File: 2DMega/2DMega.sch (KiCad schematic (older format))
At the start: 40 parts, among them J1 Conn_01x04_Male, J2 Conn_01x04_Female, J3 Conn_01x04_Male, J4 Conn_01x04_Female, P1 Power, P10 CONN_01X01, P11 CONN_01X01, P12 CONN_01X01, P13 CONN_01X01, P2 Analog, P3 Analog, P4 Digital, P5 PWM, P6 PWM, P7 Communication, P8 CONN_01X01, P9 CONN_01X01, U1 HDSP-A153

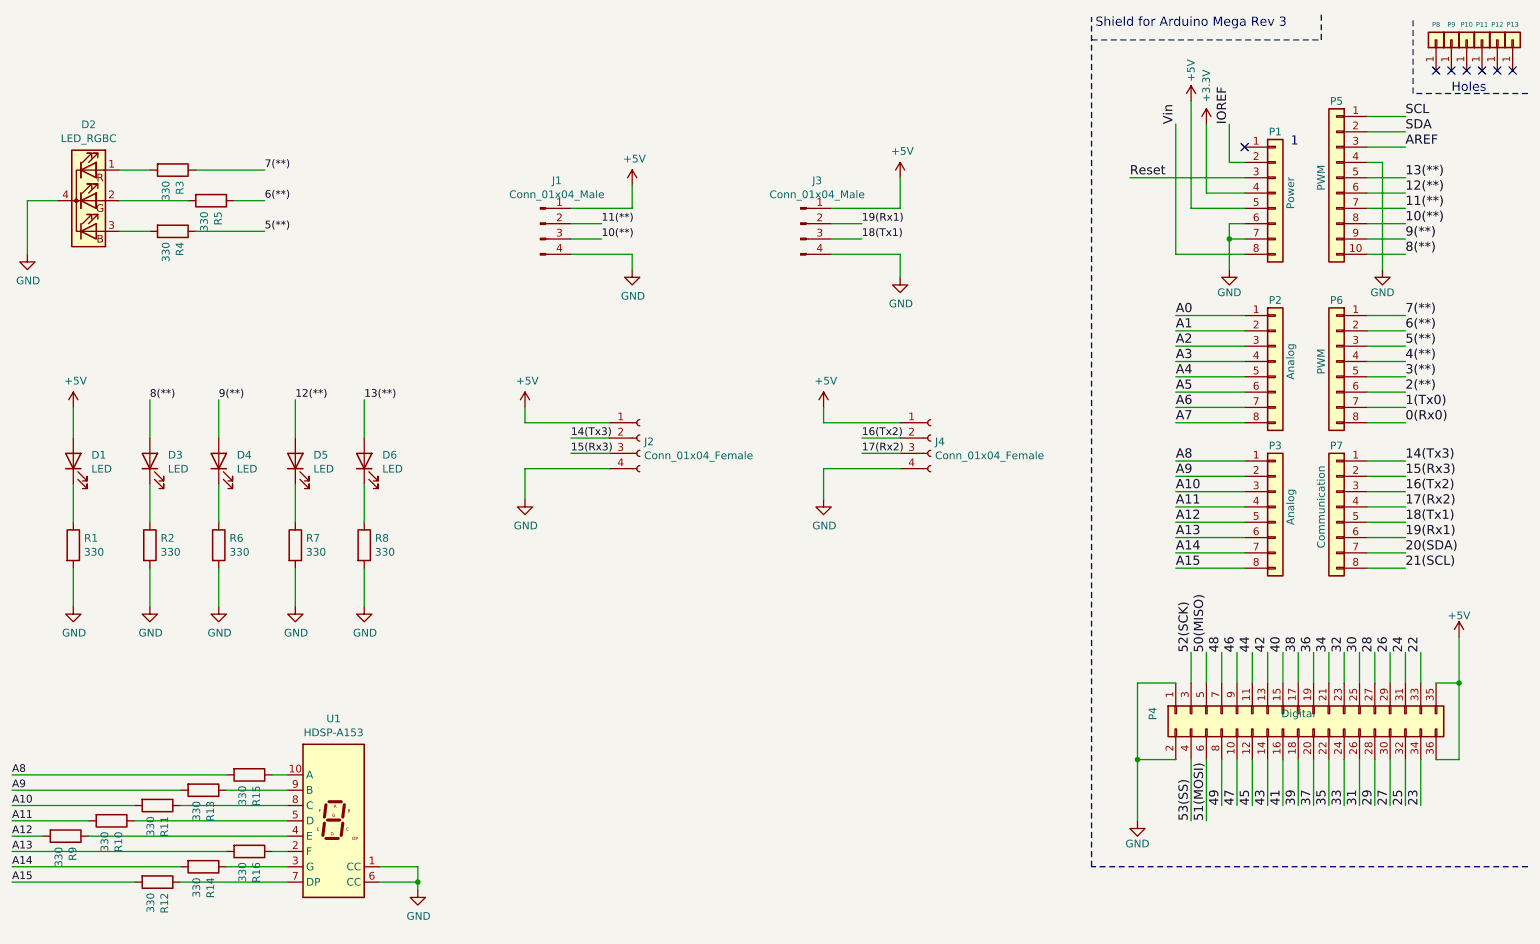
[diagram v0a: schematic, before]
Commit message: Changed to square
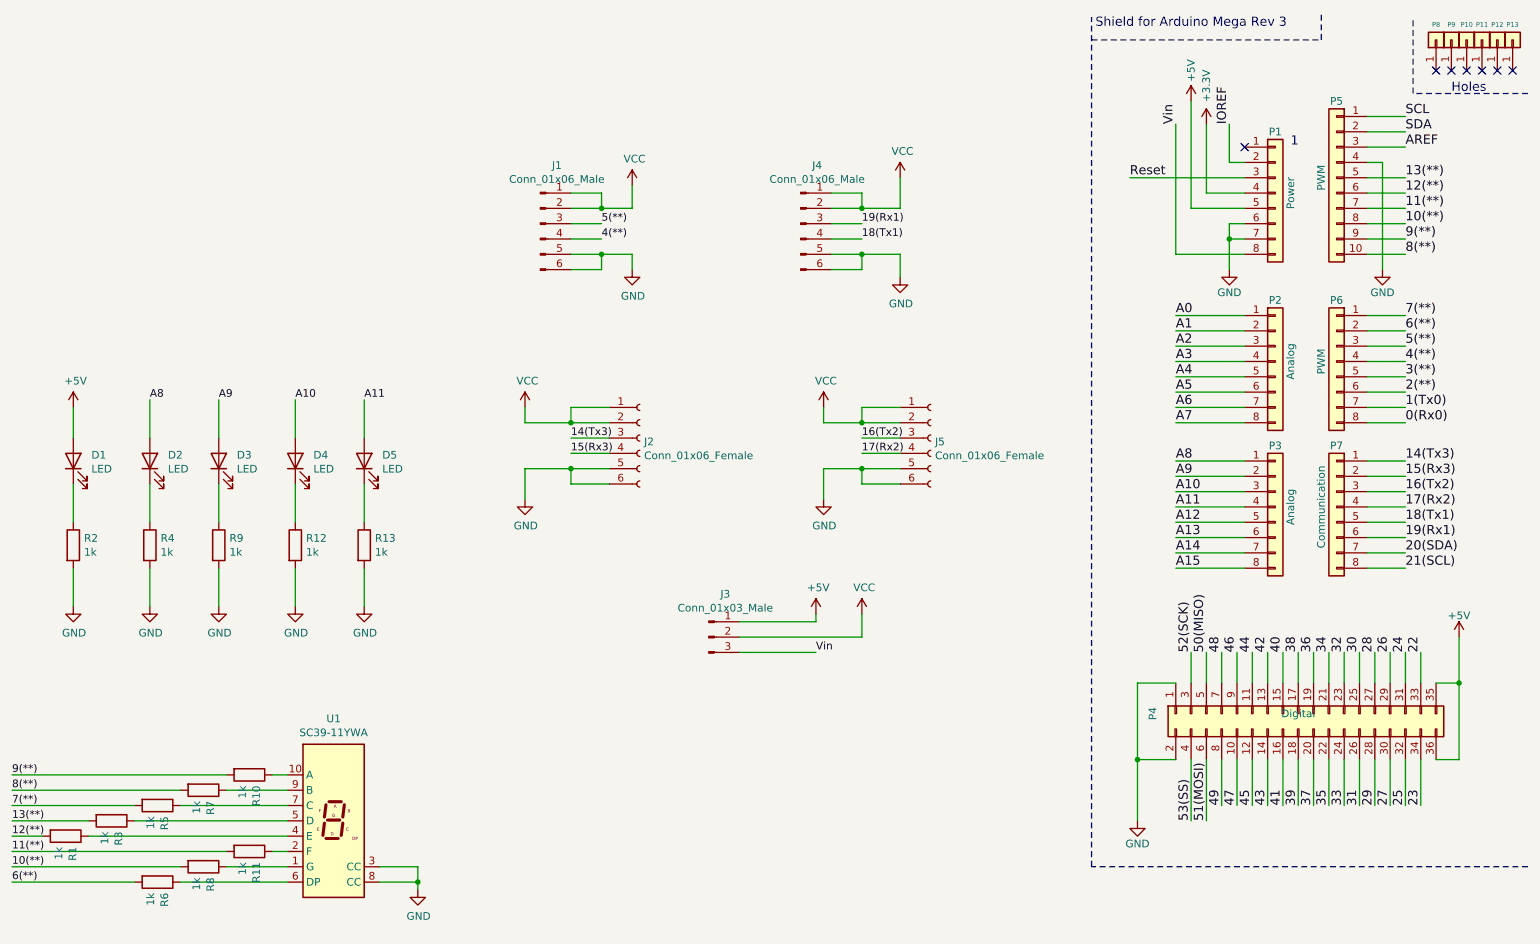
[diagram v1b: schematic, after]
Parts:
- removed D2: LED_RGBC, LED_THT:LED_D5.0mm-4_RGB, symbol Device:LED_RGBC
- removed J1, J3: Conn_01x04_Male, Connector_PinHeader_2.54mm:PinHeader_1x04_P2.54mm_Horizontal, symbol Connector:Conn_01x04_Male
- removed J2, J4: Conn_01x04_Female, Connector_PinSocket_2.54mm:PinSocket_1x04_P2.54mm_Horizontal, symbol Connector:Conn_01x04_Female
- removed R3, R4, R5: 330, Resistor_THT:R_Axial_DIN0207_L6.3mm_D2.5mm_P10.16mm_Horizontal, symbol Device:R
- removed U1: HDSP-A153, Display_7Segment:HDSP-A151, symbol Display_Character:HDSP-A153
- added J1, J4: Conn_01x06_Male, Connector_PinHeader_2.54mm:PinHeader_1x06_P2.54mm_Horizontal, symbol Connector:Conn_01x06_Male
- added J2, J5: Conn_01x06_Female, Connector_PinSocket_2.54mm:PinSocket_1x06_P2.54mm_Horizontal, symbol Connector:Conn_01x06_Female
- added J3: Conn_01x03_Male, Connector_PinHeader_2.54mm:PinHeader_1x03_P2.54mm_Vertical, symbol Connector:Conn_01x03_Male
- added U1: SC39-11YWA, Display_7Segment:Sx39-1xxxxx, symbol Display_Character:SC39-11YWA
- D1: footprint LED_THT:LED_D5.0mm -> LED_SMD:LED_0805_2012Metric_Pad1.15x1.40mm_HandSolder
- D2: renamed from D3; footprint LED_THT:LED_D5.0mm -> LED_SMD:LED_0805_2012Metric_Pad1.15x1.40mm_HandSolder
- D3: renamed from D4; footprint LED_THT:LED_D5.0mm -> LED_SMD:LED_0805_2012Metric_Pad1.15x1.40mm_HandSolder
- D4: renamed from D5; footprint LED_THT:LED_D5.0mm -> LED_SMD:LED_0805_2012Metric_Pad1.15x1.40mm_HandSolder
- D5: renamed from D6; footprint LED_THT:LED_D5.0mm -> LED_SMD:LED_0805_2012Metric_Pad1.15x1.40mm_HandSolder
- R1: renamed from R9; value 330 -> 1k; footprint Resistor_THT:R_Axial_DIN0207_L6.3mm_D2.5mm_P10.16mm_Horizontal -> Resistor_SMD:R_0805_2012Metric_Pad1.20x1.40mm_HandSolder
- R10: renamed from R15; value 330 -> 1k; footprint Resistor_THT:R_Axial_DIN0207_L6.3mm_D2.5mm_P10.16mm_Horizontal -> Resistor_SMD:R_0805_2012Metric_Pad1.20x1.40mm_HandSolder
- R11: renamed from R16; value 330 -> 1k; footprint Resistor_THT:R_Axial_DIN0207_L6.3mm_D2.5mm_P10.16mm_Horizontal -> Resistor_SMD:R_0805_2012Metric_Pad1.20x1.40mm_HandSolder
- R12: renamed from R7; value 330 -> 1k; footprint Resistor_THT:R_Axial_DIN0207_L6.3mm_D2.5mm_P10.16mm_Horizontal -> Resistor_SMD:R_0805_2012Metric_Pad1.20x1.40mm_HandSolder
- R13: renamed from R8; value 330 -> 1k; footprint Resistor_THT:R_Axial_DIN0207_L6.3mm_D2.5mm_P10.16mm_Horizontal -> Resistor_SMD:R_0805_2012Metric_Pad1.20x1.40mm_HandSolder
- R2: renamed from R1; value 330 -> 1k; footprint Resistor_THT:R_Axial_DIN0207_L6.3mm_D2.5mm_P10.16mm_Horizontal -> Resistor_SMD:R_0805_2012Metric_Pad1.20x1.40mm_HandSolder
- R3: renamed from R10; value 330 -> 1k; footprint Resistor_THT:R_Axial_DIN0207_L6.3mm_D2.5mm_P10.16mm_Horizontal -> Resistor_SMD:R_0805_2012Metric_Pad1.20x1.40mm_HandSolder
- R4: renamed from R2; value 330 -> 1k; footprint Resistor_THT:R_Axial_DIN0207_L6.3mm_D2.5mm_P10.16mm_Horizontal -> Resistor_SMD:R_0805_2012Metric_Pad1.20x1.40mm_HandSolder
- R5: renamed from R11; value 330 -> 1k; footprint Resistor_THT:R_Axial_DIN0207_L6.3mm_D2.5mm_P10.16mm_Horizontal -> Resistor_SMD:R_0805_2012Metric_Pad1.20x1.40mm_HandSolder
- R6: renamed from R12; value 330 -> 1k; footprint Resistor_THT:R_Axial_DIN0207_L6.3mm_D2.5mm_P10.16mm_Horizontal -> Resistor_SMD:R_0805_2012Metric_Pad1.20x1.40mm_HandSolder
- R7: renamed from R13; value 330 -> 1k; footprint Resistor_THT:R_Axial_DIN0207_L6.3mm_D2.5mm_P10.16mm_Horizontal -> Resistor_SMD:R_0805_2012Metric_Pad1.20x1.40mm_HandSolder
- R8: renamed from R14; value 330 -> 1k; footprint Resistor_THT:R_Axial_DIN0207_L6.3mm_D2.5mm_P10.16mm_Horizontal -> Resistor_SMD:R_0805_2012Metric_Pad1.20x1.40mm_HandSolder
- R9: renamed from R6; value 330 -> 1k; footprint Resistor_THT:R_Axial_DIN0207_L6.3mm_D2.5mm_P10.16mm_Horizontal -> Resistor_SMD:R_0805_2012Metric_Pad1.20x1.40mm_HandSolder
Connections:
- net +5V: now also J3.1 (Pin_1)
- net 10(**): now also R8.2
- net 11(**): now also R11.2
- net 12(**): now also R1.2; no longer D4.2 (A)
- net 13(**): now also R3.2; no longer D5.2 (A)
- net 14(Tx3): now also J2.3 (Pin_3)
- net 15(Rx3): now also J2.4 (Pin_4)
- net 16(Tx2): now also J5.3 (Pin_3)
- net 17(Rx2): now also J5.4 (Pin_4)
- net 18(Tx1): now also J4.4 (Pin_4)
- net 19(Rx1): now also J4.3 (Pin_3)
- net 4(**): now also J1.4 (Pin_4)
- net 5(**): now also J1.3 (Pin_3)
- net 6(**): now also R6.2
- net 7(**): now also R5.2
- net 8(**): now also R7.2; no longer D2.2 (A)
- net 9(**): now also R10.2; no longer D3.2 (A)
- net A10: now also D4.2 (A); no longer R5.2
- net A11: now also D5.2 (A); no longer R3.2
- net A12: no longer R1.2
- net A13: no longer R11.2
- net A14: no longer R8.2
- net A15: no longer R6.2
- net A8: now also D2.2 (A); no longer R10.2
- net A9: now also D3.2 (A); no longer R7.2
- net GND: now also J1.5 (Pin_5), J1.6 (Pin_6), J2.5 (Pin_5), J2.6 (Pin_6), J4.5 (Pin_5), J4.6 (Pin_6), J5.5 (Pin_5), J5.6 (Pin_6), U1.3 (CC), U1.8 (CC)
- net Vin: now also J3.3 (Pin_3)
- net at R10.1: now also U1.10 (A)
- net at R11.1: now also U1.2 (F)
- net at R8.1: now also U1.1 (G)
- net at R1.1: now also U1.4 (E)
- net at R3.1: now also U1.5 (D)
- net at R6.1: now also U1.6 (DP)
- net at R5.1: now also U1.7 (C)
- net at R7.1: now also U1.9 (B)
- new net VCC: J1.1 (Pin_1), J1.2 (Pin_2), J2.1 (Pin_1), J2.2 (Pin_2), J3.2 (Pin_2), J4.1 (Pin_1), J4.2 (Pin_2), J5.1 (Pin_1), J5.2 (Pin_2)

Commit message: Added RGB_LED, reorganized pins
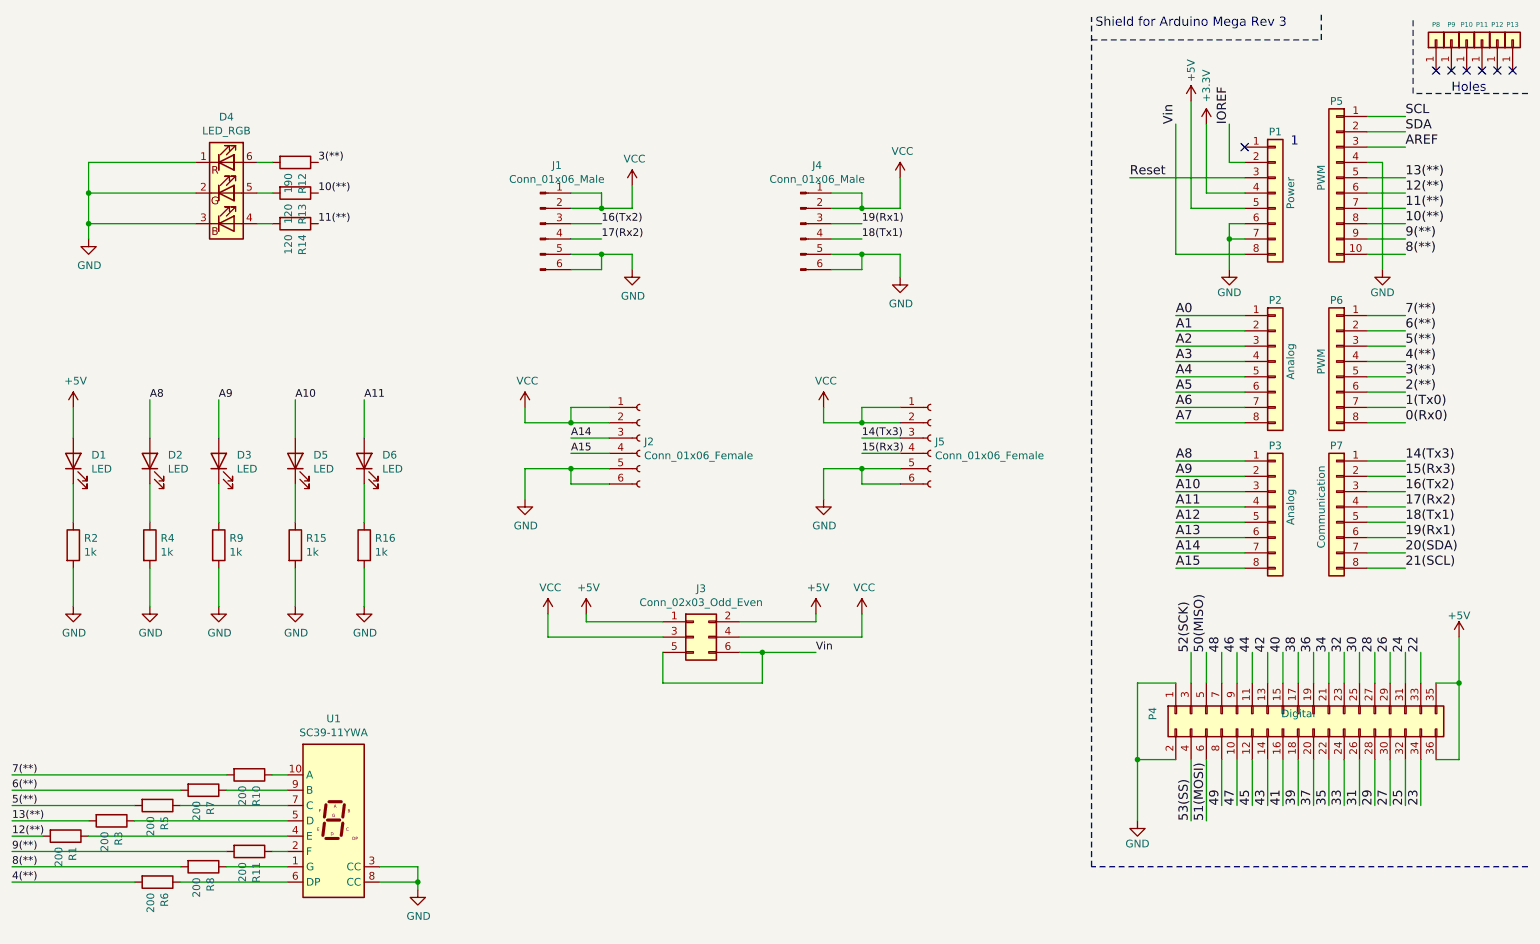
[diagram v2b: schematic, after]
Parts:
- removed J3: Conn_01x03_Male, Connector_PinHeader_2.54mm:PinHeader_1x03_P2.54mm_Vertical, symbol Connector:Conn_01x03_Male
- added D4: LED_RGB, LED_SMD:LED_Avago_PLCC6_3x2.8mm, symbol Device:LED_RGB
- added J3: Conn_02x03_Odd_Even, Connector_PinHeader_2.54mm:PinHeader_2x03_P2.54mm_Vertical, symbol Connector_Generic:Conn_02x03_Odd_Even
- added R12: 190, Resistor_SMD:R_0805_2012Metric_Pad1.20x1.40mm_HandSolder, symbol Device:R
- added R13, R14: 120, Resistor_SMD:R_0805_2012Metric_Pad1.20x1.40mm_HandSolder, symbol Device:R
- R1, R10, R11, R3, R5, R6, R7, R8: value 1k -> 200
- renumbered D4 to D5, D5 to D6, R12 to R15, R13 to R16
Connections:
- net +5V: now also J3.1 (Pin_1), J3.2 (Pin_2)
- net 10(**): now also R13.1; no longer R8.2
- net 11(**): now also R14.1; no longer R11.2
- net 14(Tx3): now also J5.3 (Pin_3); no longer J2.3 (Pin_3)
- net 15(Rx3): now also J5.4 (Pin_4); no longer J2.4 (Pin_4)
- net 16(Tx2): now also J1.3 (Pin_3); no longer J5.3 (Pin_3)
- net 17(Rx2): now also J1.4 (Pin_4); no longer J5.4 (Pin_4)
- net 3(**): now also R12.1
- net 4(**): now also R6.2; no longer J1.4 (Pin_4)
- net 5(**): now also R5.2; no longer J1.3 (Pin_3)
- net 6(**): now also R7.2; no longer R6.2
- net 7(**): now also R10.2; no longer R5.2
- net 8(**): now also R8.2; no longer R7.2
- net 9(**): now also R11.2; no longer R10.2
- net A14: now also J2.3 (Pin_3)
- net A15: now also J2.4 (Pin_4)
- net GND: now also D4.1 (RK), D4.2 (GK), D4.3 (BK)
- net VCC: now also J3.3 (Pin_3), J3.4 (Pin_4)
- net Vin: now also J3.5 (Pin_5), J3.6 (Pin_6)
- new net: D4.6 (RA), R12.2
- new net: D4.5 (GA), R13.2
- new net: D4.4 (BA), R14.2
